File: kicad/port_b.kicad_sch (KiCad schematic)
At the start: 1 part, among them U162 74LS367

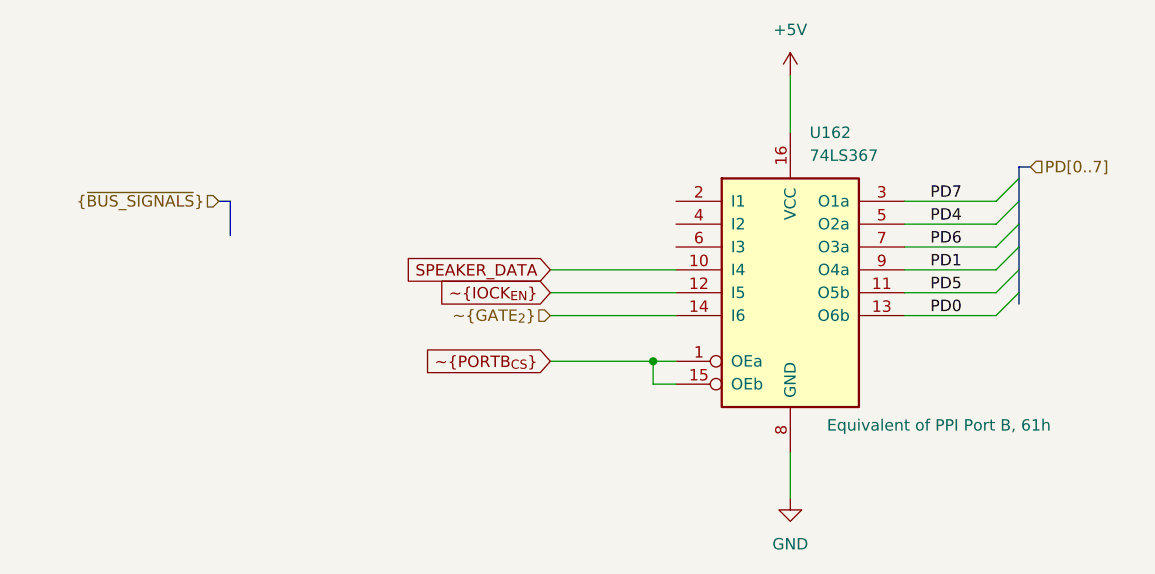
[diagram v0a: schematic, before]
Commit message: Fixes to clocks,  keyboard controller stuff.
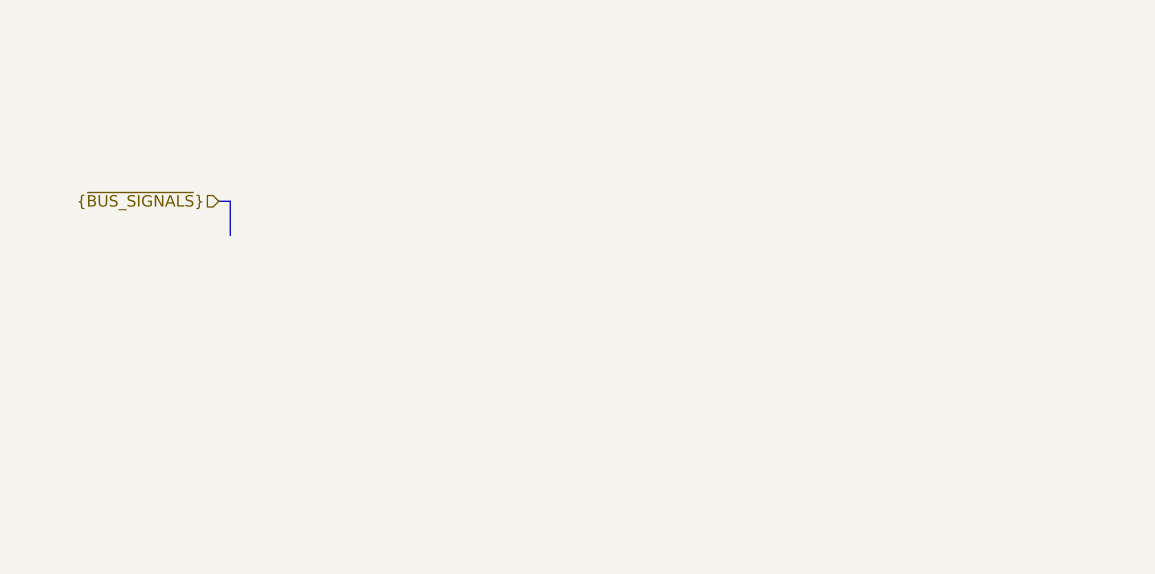
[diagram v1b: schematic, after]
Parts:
- removed U162: 74LS367, Package_DIP:DIP-16_W7.62mm, symbol 74xx:74LS367
